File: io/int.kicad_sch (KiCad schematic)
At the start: 43 parts, among them J1 Conn_02x11_Top_Bottom, J16 Conn_01x02, J18 Conn_02x05_Top_Bottom, J9 Conn_01x04, Q2 Q_NPN, Q3 Q_PNP

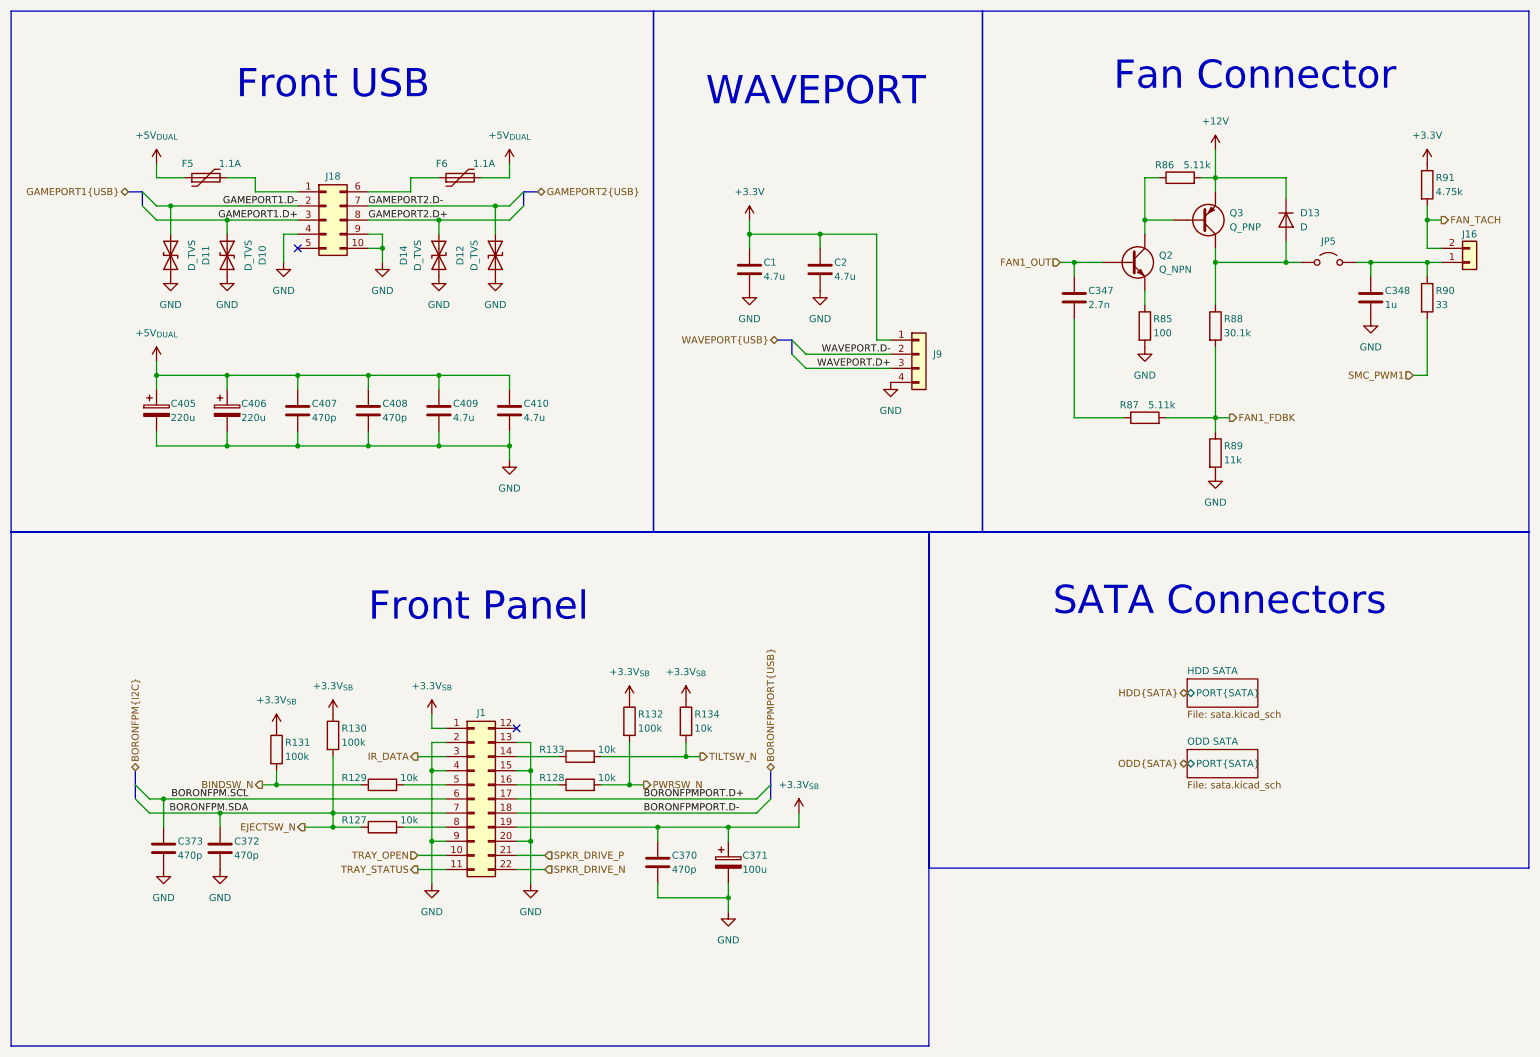
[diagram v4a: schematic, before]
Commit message: Multipurpose and standby power rails, Reannotated schematic
Added V_1P2, V_1P8, V_5P0DUAL, V_EFUSE, V_GPUPCIE, V_3P3STBY and V_1P2STBY
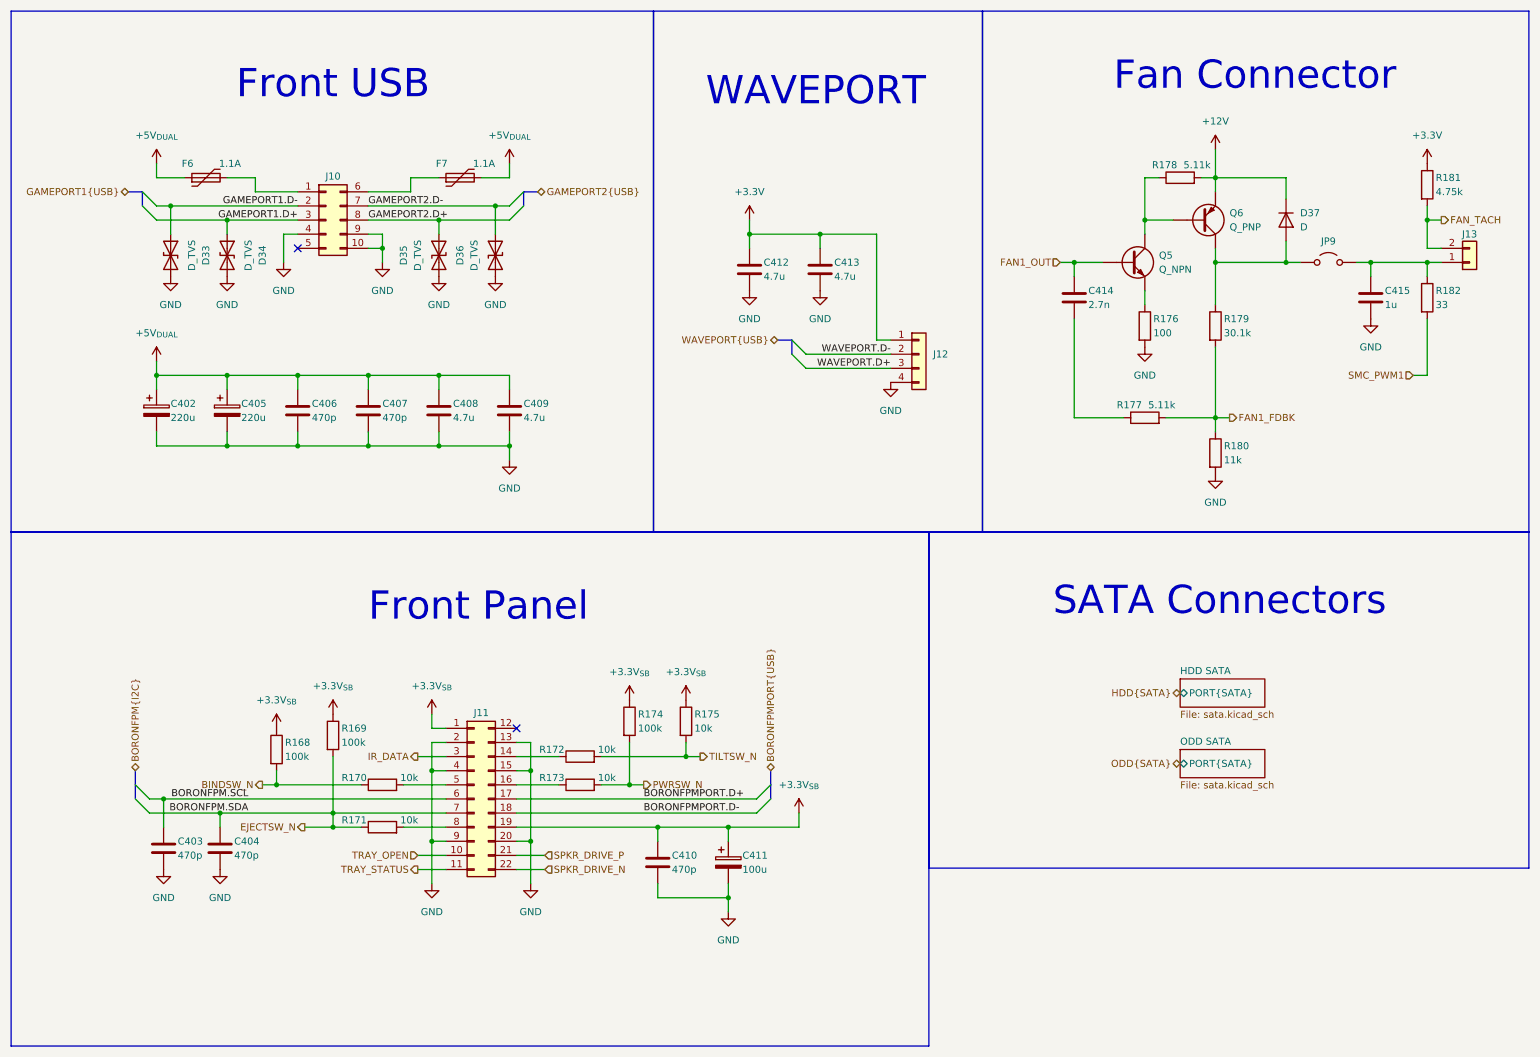
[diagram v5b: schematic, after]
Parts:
- renumbered C405 to C402, C373 to C403, C372 to C404, C406 to C405, C407 to C406, C408 to C407, C409 to C408, C410 to C409, C370 to C410, C371 to C411, C1 to C412, C2 to C413, C347 to C414, C348 to C415, D11 to D33, D10 to D34, D14 to D35, D12 to D36, D13 to D37, F5 to F6, F6 to F7, J18 to J10, J1 to J11, J9 to J12, J16 to J13, JP5 to JP9, Q2 to Q5, Q3 to Q6, R131 to R168, R130 to R169, R129 to R170, R127 to R171, R133 to R172, R128 to R173, R132 to R174, R134 to R175, R85 to R176, R87 to R177, R86 to R178, R88 to R179, R89 to R180, R91 to R181, R90 to R182
